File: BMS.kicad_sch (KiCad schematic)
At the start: 59 parts, among them J1 Screw_Terminal_01x02, J5 BATT_PACK -, J6 BATT_PACK -, Q22 CSD19531Q5A, Q23 CSD19531Q5A, Q24 CSD19531Q5A, T3 EE20_10_6_750811647, U1 TL431DBZ, U18 VIPer26LD, U2 PC817, U21 BQ7790500PWR

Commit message: Update
updated Flyback control
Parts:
- removed 2W,5.1Ohm10, 2W,5.1Ohm8, 2W,5.1Ohm9: R, Resistor_THT:R_Axial_DIN0414_L11.9mm_D4.5mm_P15.24mm_Horizontal, symbol Device:R
- removed C22: 22qf, Capacitor_THT:CP_Radial_D5.0mm_P2.00mm, symbol Device:C
- added 1/8W,33KOhm10, 1/8W,33KOhm9, 2W,4.7KOhm1, 2W,5.1Ohm11: R, Resistor_THT:R_Axial_DIN0414_L11.9mm_D4.5mm_P15.24mm_Horizontal, symbol Device:R
- added C1, C2: 470uF/20V, Capacitor_SMD:C_0805_2012Metric, symbol Device:C_Polarized
- added C23: 22qf, Capacitor_THT:CP_Radial_D5.0mm_P2.00mm, symbol Device:C
- added C24: 4.7nF, Capacitor_THT:CP_Radial_D5.0mm_P2.00mm, symbol Device:C
- added D1: BZV55B18, Diode_SMD:D_MiniMELF, symbol Diode:BZV55B18
- C21: value 22qf -> 2.2nf
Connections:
- net GND: now also U1.3 (A), 1/8W,33KOhm9.1, C1.2, C2.2, C23.2, C24.2, D1.2 (A); no longer 2W,5.1Ohm7.2, D4.1 (K), U2.2
- net at U2.1: now also 2W,5.1Ohm11.1; no longer U18.7 (FB)
- net at U2.3: now also C23.1
- net FB: now reaches U2.4
- net FB: now also U18.7 (FB), C24.1
- net at C21.1: now also U1.2 (REF), 1/8W,33KOhm10.1, 1/8W,33KOhm9.2, 2W,5.1Ohm11.2; no longer U1.1 (K)
- net at C21.2: now also 2W,4.7KOhm1.2
- new net: 2W,4.7KOhm1.1, U1.1 (K), U2.2
- new net VO: 1/8W,33KOhm10.2, 2W,5.1Ohm7.2, C1.1, C2.1, D1.1 (K), D4.1 (K)
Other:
- moved on the sheet: 1M3, 1M5, 220ohm, 220ohm1, 2W,5.1Ohm, 2W,5.1Ohm1, 2W,5.1Ohm13, 2W,5.1Ohm17, 2W,5.1Ohm18, 2W,5.1Ohm19, 2W,5.1Ohm2, 2W,5.1Ohm20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

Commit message: update schematic view
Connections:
- net at 2W,5.1Ohm11.1: now also 1/8W,33KOhm10.1, 1/8W,33KOhm9.2, C21.1, U1.2 (REF); no longer U2.1
- new net: 2W,5.1Ohm11.2, U2.1
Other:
- moved on the sheet: 1/8W,33KOhm10, 2W,5.1Ohm, 2W,5.1Ohm11, 2W,5.1Ohm6, 2W,5.1Ohm7, C1, C2, C20, C33, C34, C35, C38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

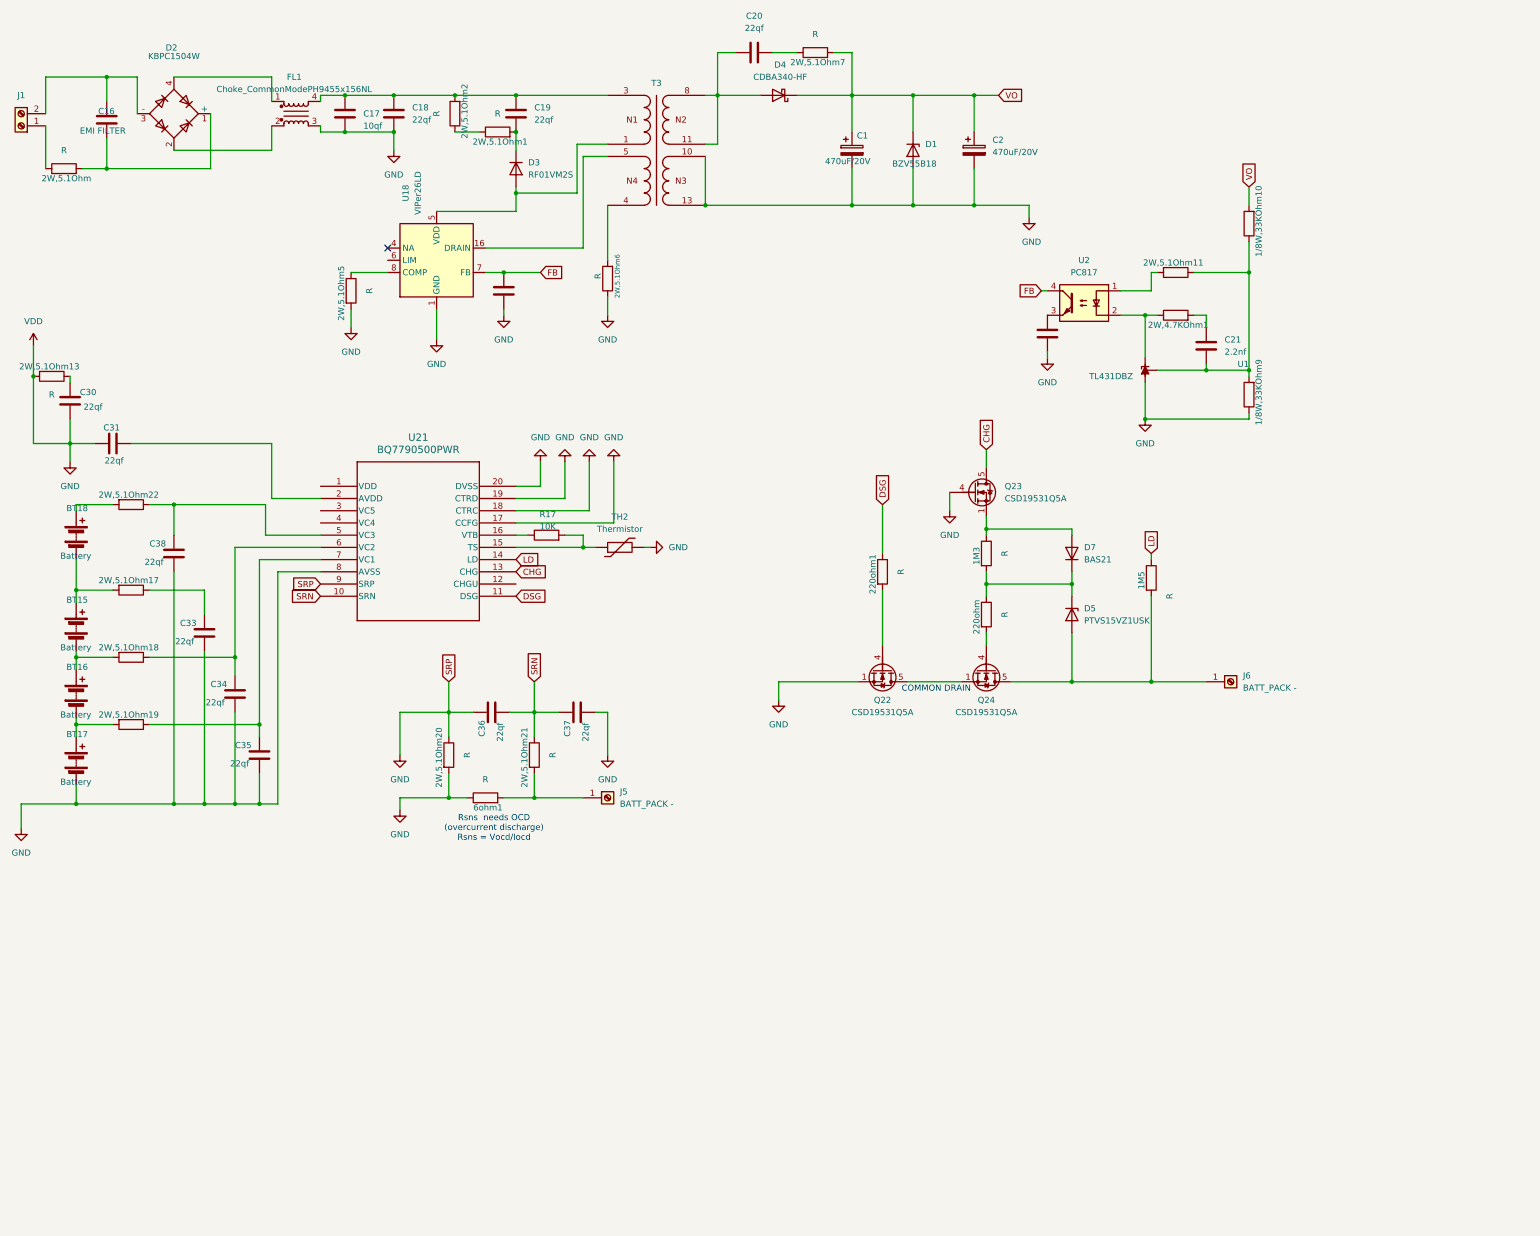
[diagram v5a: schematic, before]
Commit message: Add AC/DC & balancer sheets; update BMS schematic
Add new schematic files (acdc, acdcflyback, acdc.sch.kicad_sch, balancer/balance, overcharge, overcurrent) plus autosave copies, a backup zip and KiCad lock files. Update BMS.kicad_pro to register the new sheets and populate used_designators. Update BMS.kicad_sch: change paper size A4->A3, add header text annotations (AC/DC and battery balance), and reposition many components/junctions/wires to accommodate the expanded layout.
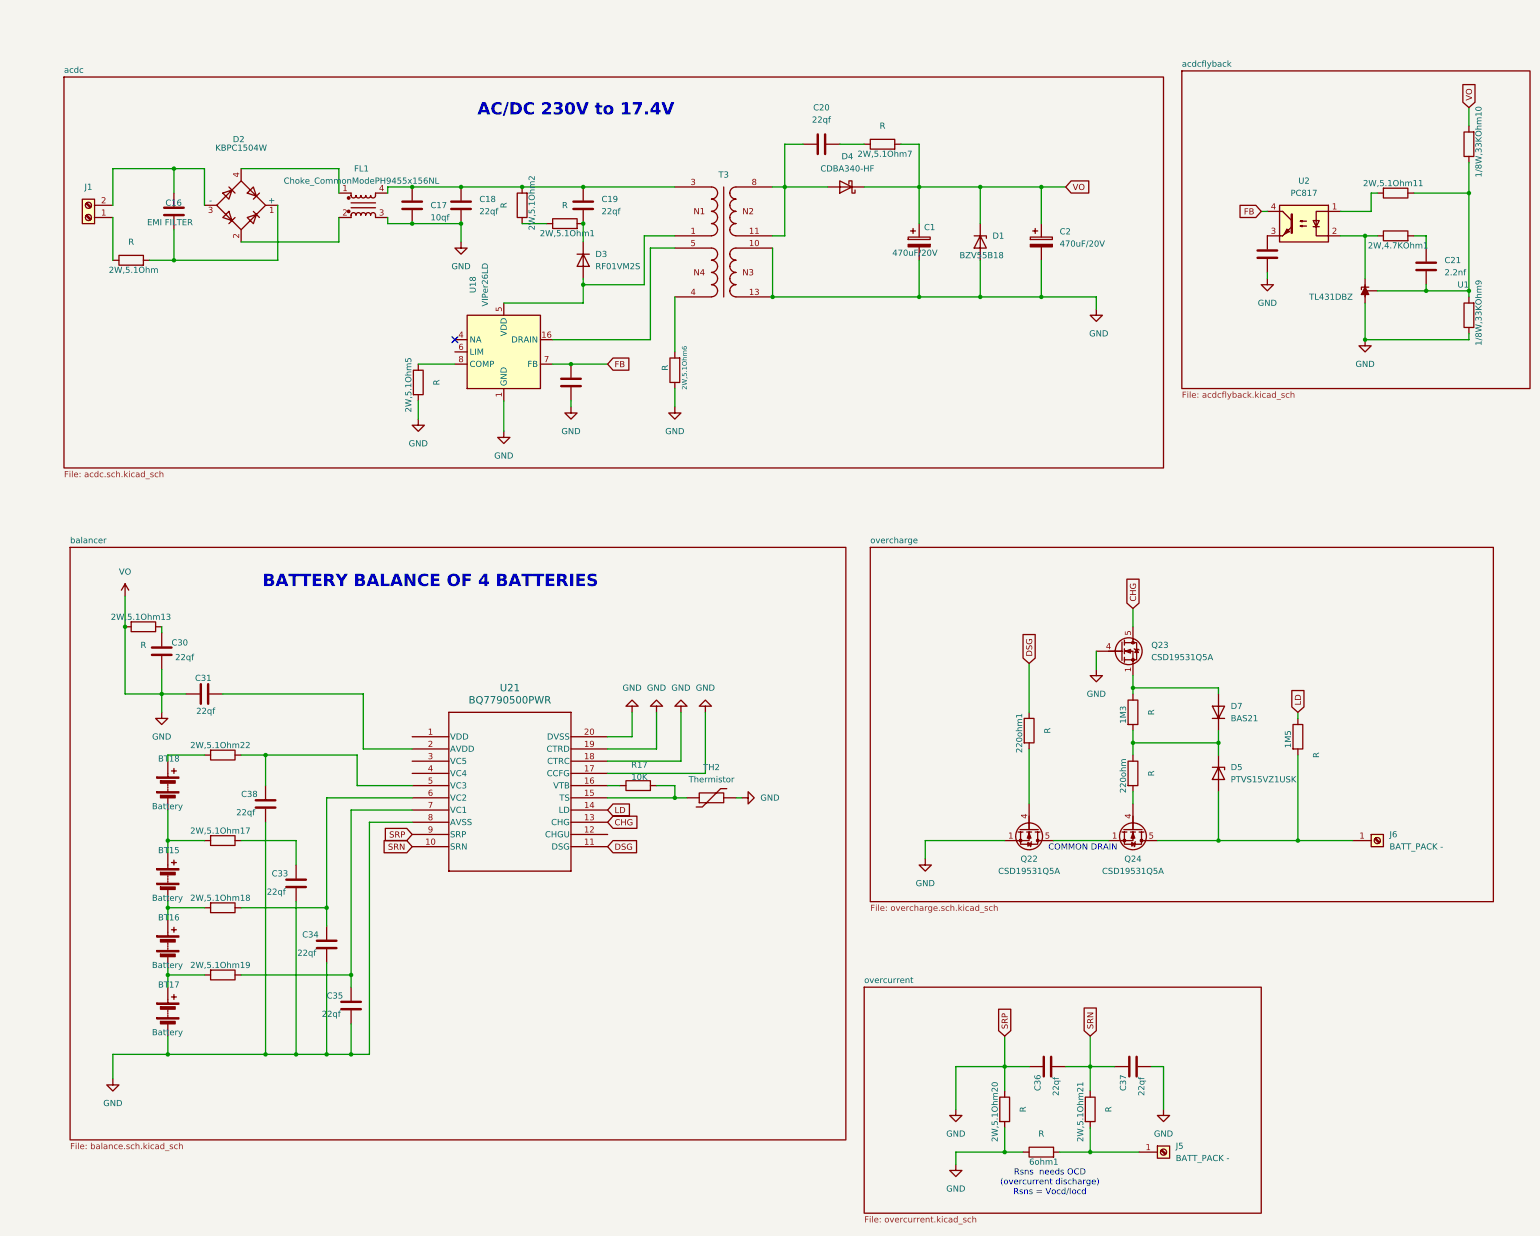
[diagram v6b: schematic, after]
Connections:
- net VO is gone; now on net GND: 1/8W,33KOhm10.2, 2W,5.1Ohm7.2, C1.1, C2.1, D1.1 (K), D4.1 (K)
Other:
- added sheet acdc (acdc.sch.kicad_sch)
- added sheet acdcflyback (acdcflyback.kicad_sch)
- added sheet balancer (balance.sch.kicad_sch)
- added sheet overcharge (overcharge.sch.kicad_sch)
- added sheet overcurrent (overcurrent.kicad_sch)
- note added: "AC/DC 230V to 17.4V"
- note added: "BATTERY BALANCE OF 4 BATTERIES"
- moved on the sheet: 1/8W,33KOhm10, 1/8W,33KOhm9, 1M3, 1M5, 220ohm, 220ohm1, 2W,4.7KOhm1, 2W,5.1Ohm, 2W,5.1Ohm1, 2W,5.1Ohm11, 2W,5.1Ohm13, 2W,5.1Ohm17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

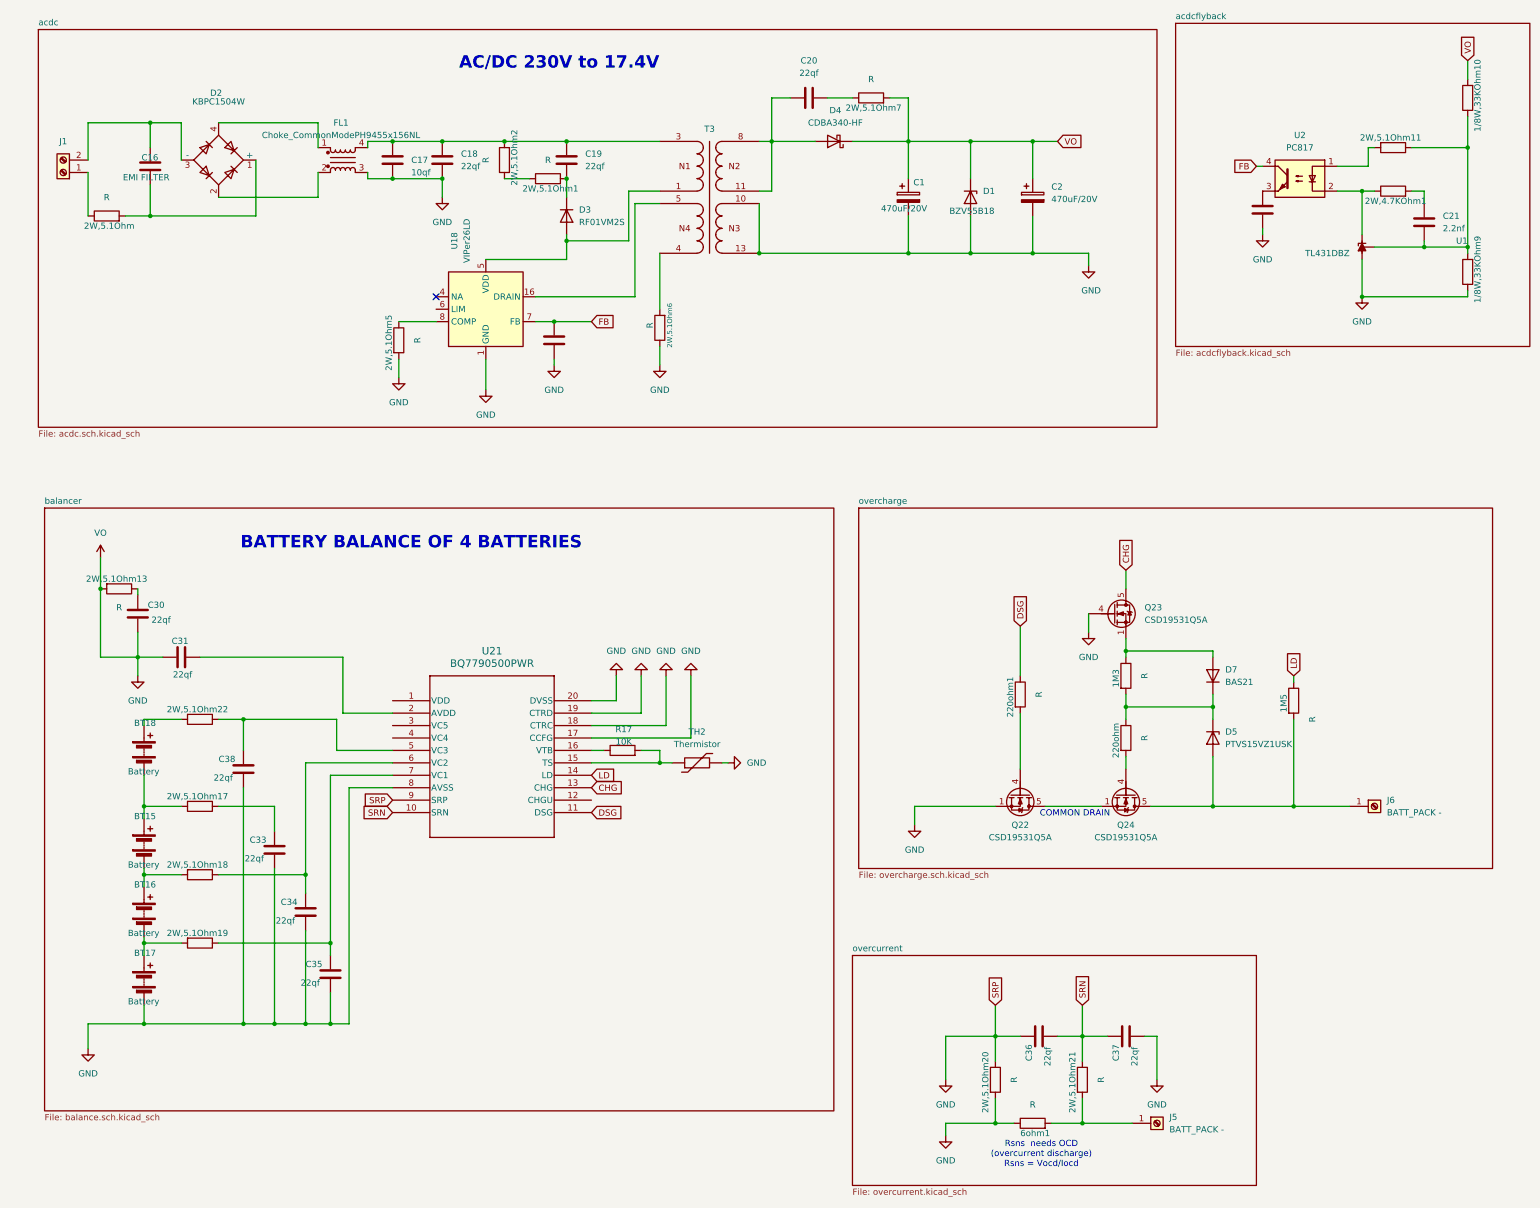
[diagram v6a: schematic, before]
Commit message: Add EMI filter symbol; adjust schematic labels/wiring
Add two backup ZIPs and update KiCad project/schematic. BMS.kicad_pro: add ngspice config, simplify used_designators and trim sheets list. BMS.kicad_sch: add a new EMI filter symbol (P300PL104M275xC332) with graphics and pins, adjust many wires/junctions/no_connects, reposition and add global labels (FB, VDD, DSG, SRN, VO, CHG), update several power/GND symbols and component references/values/footprints (including renaming inrush resistor and R1), plus other cleanup of instances and UUIDs. These changes prepare the schematic for the EMI component and tidy net labeling/placement.
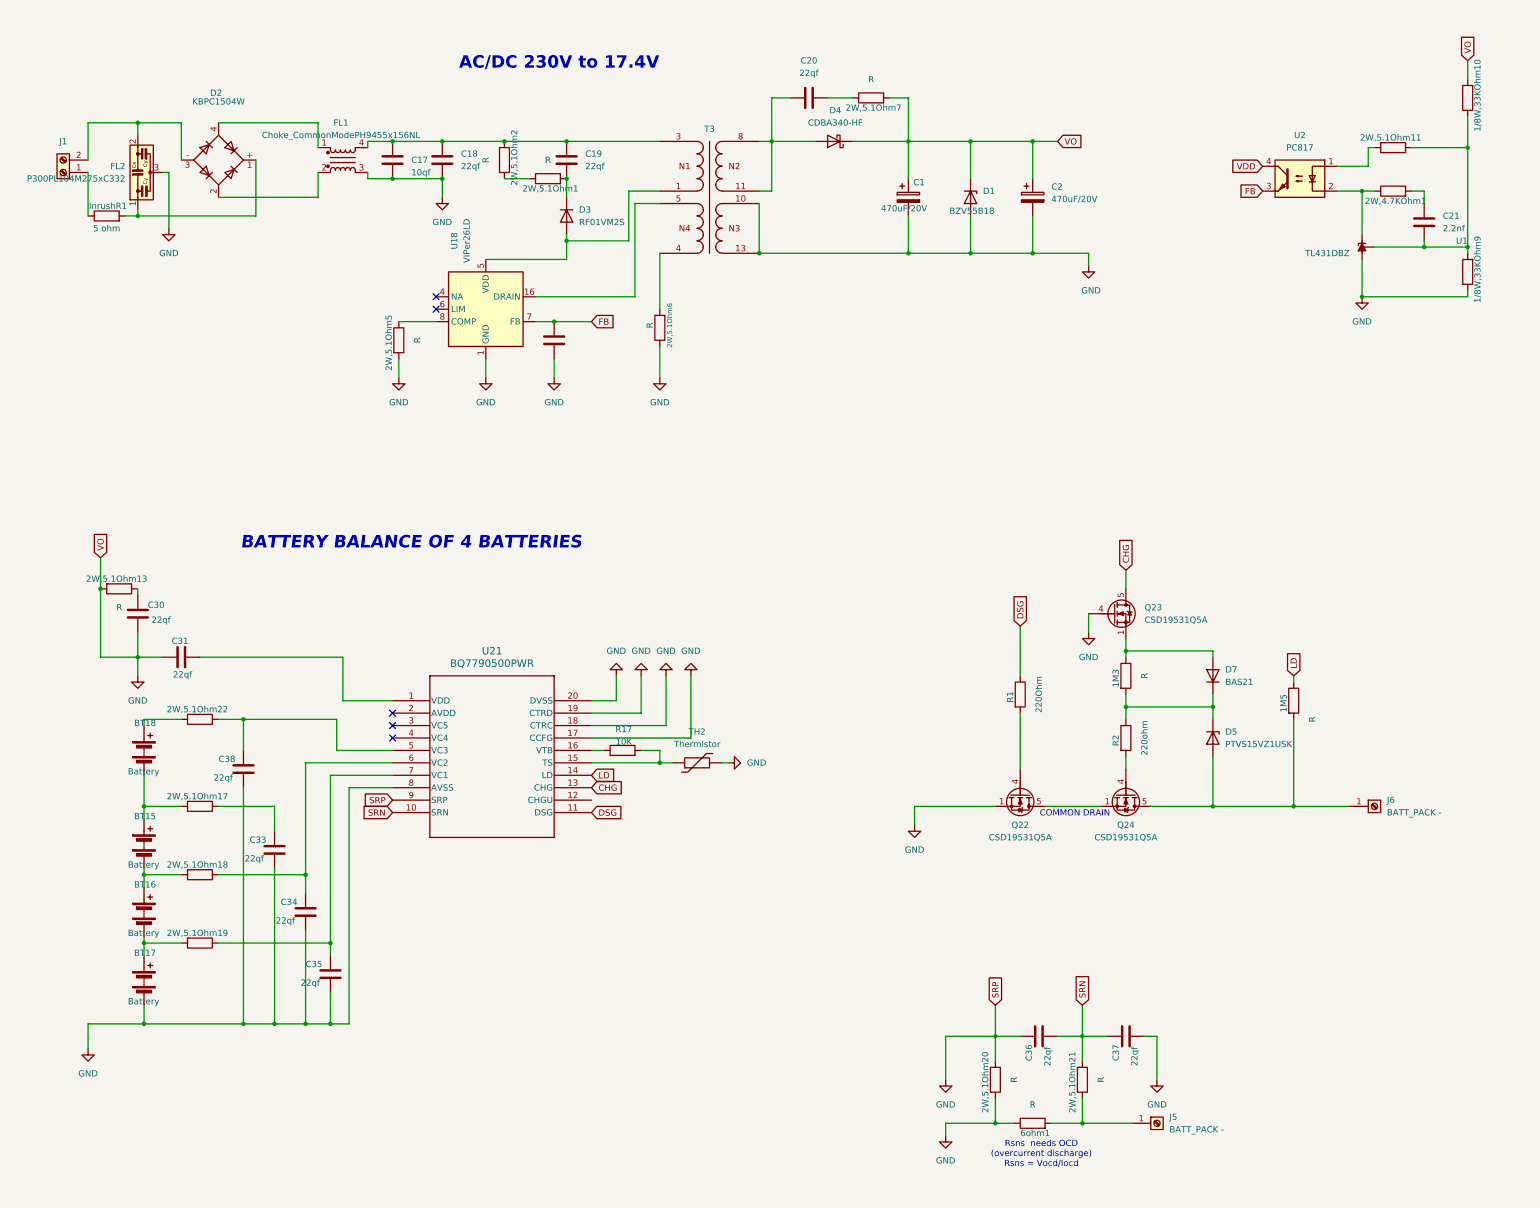
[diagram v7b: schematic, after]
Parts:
- removed C16: EMI FILTER, symbol Device:C
- removed C23: 22qf, Capacitor_THT:CP_Radial_D5.0mm_P2.00mm, symbol Device:C
- added FL2: P300PL104M275xC332, Filter:Filter_KEMET_PZB300_24.0x12.5mm_P10.0mm, symbol Filter:P300PL104M275xC332
- BT15, BT16, BT17, BT18: footprint (none) -> Battery:BatteryHolder_Keystone_2460_1xAA
- InrushR1: renamed from 2W,5.1Ohm; value R -> 5 ohm; footprint Resistor_THT:R_Axial_DIN0414_L11.9mm_D4.5mm_P15.24mm_Horizontal -> Resistor_THT:R_Axial_DIN0414_L11.9mm_D4.5mm_P25.40mm_Horizontal
- R1: renamed from 220ohm1; value R -> 220Ohm
- R2: renamed from 220ohm; value R -> 220ohm
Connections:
- net FB: now also U2.3; no longer U2.4
- net GND: now also FL2.3
- net at D2.1 (+), InrushR1.2: now also FL2.1
- net at D2.3 (-), J1.2 (Pin_2): now also FL2.2
- net at C31.2: now also U21.1 (VDD); no longer U21.2 (AVDD)
- new net VDD: U2.4
- no-connect marks 1 -> 5
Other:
- removed sheet acdc
- removed sheet acdcflyback
- removed sheet balancer
- removed sheet overcharge
- removed sheet overcurrent
